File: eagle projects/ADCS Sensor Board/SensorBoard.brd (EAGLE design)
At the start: 91 x 91 mm, 128 parts, among them Q3 CSTCR4M00G15L99, Q5 32.768kHz, U10 LMV321, U2 ADS7841E_2K5, U3 LMV321, U5 ADS7841E_2K5, U6 REF194GSZ-REEL7, U7 TLV9054IDR, U8 LMV321

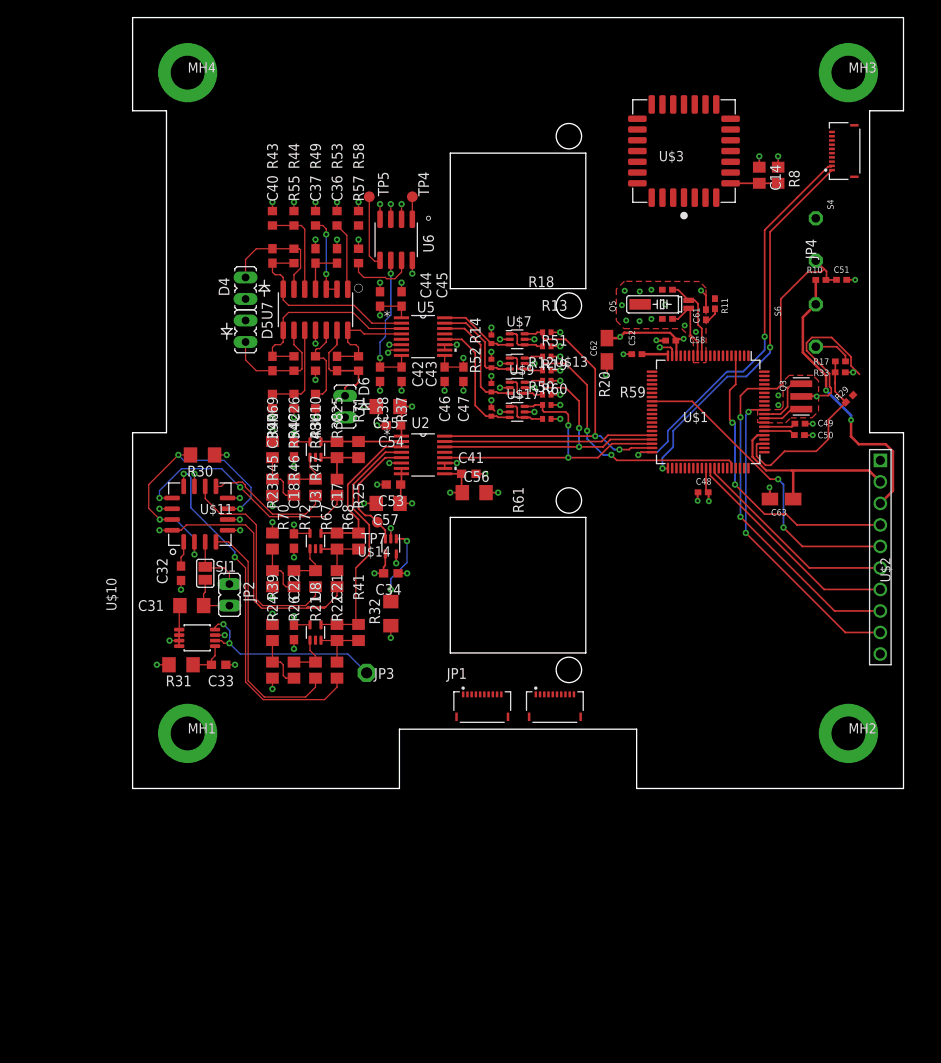
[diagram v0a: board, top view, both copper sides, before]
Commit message: Renamed sensor board files. Added notes to schematic for remaining work
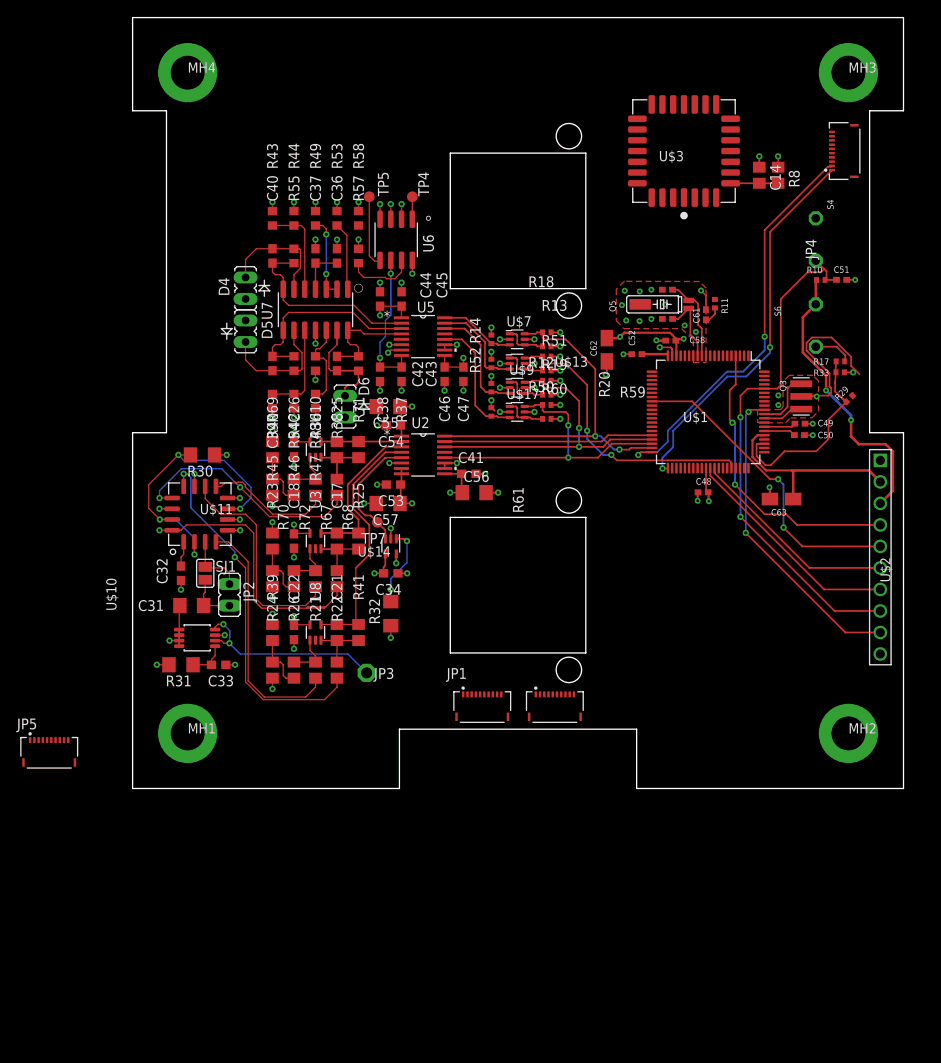
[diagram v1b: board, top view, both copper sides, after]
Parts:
- added JP5: 5034801000, my_library:MOLEX_5034801000
- R10, R11, R17, R29, R33: device rcl:0402 -> rcl:R0402
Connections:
- new net ACT_BRD_3V_PRESENT: JP4.3, JP5.1
- new net ACT_BRD_5V_PRESENT: JP4.4, JP5.2
- new net N$10: JP5.7
- new net N$17: JP5.8
- new net N$18: JP5.9
- new net N$19: JP5.10
- new net N$3: JP5.3
- new net N$4: JP5.4
- new net N$5: JP5.5
- new net N$9: JP5.6
- new net SEN_BRD_3V_PRESENT: JP4.5
- new net SEN_BRD_5V_PRESENT: JP4.6
- net GND: now also JP1.S1, JP1.S2, JP3.S1, JP3.S2, JP4.S1, JP4.S2, JP5.S1, JP5.S2

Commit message: Buncha layout done
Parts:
- removed C40: 9.1p, rcl:C0603
- removed C41, C43, C45, C46, C53, C54: 0.1u, rcl:C0603
- removed C42, C44, C47: 1u, rcl:C0603
- removed C51: 1n, rcl:0402
- removed C55, C56, C57: 1u, resistor:C1206
- removed C62: 10u, rcl:A/3216-18R
- removed D4, D5, D6: SFH2430, my_library:JP1Y_LED_SCREEN
- removed R53, R57, R58: 5.1M, rcl:R0603
- removed R54, R55: 698k, rcl:R0603
- removed R59, R60, R61: 10k, rcl:R0402
- removed R67, R68: 5.6k, rcl:R0805
- removed R69, R70: 1k, rcl:R0805
- removed R71, R72: 1.37M, rcl:R0805
- removed U$10: IRF7507TRPBF, my_library:SOP8P65_300X490X111L53X30N
- removed U$11: HMC1053, my_library:LCCS16P127_736X736X279L127X50N
- removed U$13, U$17, U$7, U$9: BSS138PS,115, my_library:SOT23-6P65_200X110L30X25N_BSS138PS,115
- removed U$14: LM20BIM7X_NOPB, my_library:SOT23-5P65_210X110L40X22N_LM20
- removed U$3: MTI-1, my_library:LCC28P127_1210X1210X260L90X63_MTI-1
- removed U10: LMV321, my_library:SOT23-5P65_210X110L36X22N
- added A1: HMC1053PA0242, my_library:PA0242
- added C10: 1n, rcl:0402
- added C12, C15, C16: 1u, resistor:C1206
- added C13, C19, C23, C30: 0.1u, rcl:C0603
- added C2: 10u, rcl:A/3216-18R
- added C20, C24, C27: 1n, rcl:C0805
- added C28: 470n, rcl:C0805
- added C29: 4.7u, rcl:C0603
- added C35: 1u, rcl:C0603
- added D1, D2, D3: SFH2430, my_library:JP1Y_LED_SCREEN
- added J6: MTI-1_8428-11B1-RK-TP, my_library:PLCC-28_SOCKET_TH
- added Q2: IRF7507TRPBF, my_library:SOP8P65_300X490X111L53X30N
- added Q4, Q6: BSS138PS,115, my_library:SOT23-6P65_200X110L30X25N_BSS138PS,115
- added R1: 0R, rcl:R0402
- added R15: 5.1M, resistor:R1206
- added R16, R9: 5.6k, rcl:R0805
- added R2: 47k, rcl:R0402
- added R27: 27R, rcl:R0805
- added R28, R34: 10k, rcl:R0402
- added R3: 1k4, rcl:R0402
- added R35: 698k, rcl:R0603
- added R4: 100R, rcl:R0402
- added R5: 1M, rcl:R0402
- added R6: 200R, resistor:R1206
- added R7: 1k, rcl:R0805
- added U4: LMV321, my_library:SOT23-5P65_210X110L36X22N
- added U9: ADS7841E_2K5, my_library:DBQ16
- added Y1: 32.768kHz, my_library:MS3V-T1R
- added Y2: CSTCR4M00G15L99, my_library:MURATA-FILTER_CSTCR
- C14: value 470n -> 0.1u; device rcl:C0805 -> rcl:C0603
- C17, C25: value 1n -> 0.1u; device rcl:C0805 -> rcl:C0603
- C21: device rcl:C0805 -> resistor:C1206
- C31: value 1n -> 9.1p; device resistor:C1206 -> rcl:C0603
- C32, C33: value 0.1u -> 9.1p
- C34: value 0.1u -> 1u
- C36: value 4.7u -> 1u
- C38, C39: value 9.1p -> 0.1u
- JP1: value 5034801000 -> (none); device my_library:MOLEX_5034801000 -> jumper:JP1
- JP2: device jumper:JP1 -> pinhead:2X05
- JP3, JP4: value 5034801000 -> (none); device my_library:MOLEX_5034801000 -> pinhead:2X05
- JP5: value 5034801000 -> (none); device my_library:MOLEX_5034801000 -> pinhead:1X04
- Q3: value CSTCR4M00G15L99 -> BSS138PS,115; device murata:MURATA-FILTER_CSTCR -> my_library:SOT23-6P65_200X110L30X25N_BSS138PS,115
- Q5: value 32.768kHz -> BSS138PS,115; device microcrystal:MS3V-T1R -> my_library:SOT23-6P65_200X110L30X25N_BSS138PS,115
- R10: value 47k -> 5.6k; device rcl:R0402 -> rcl:R0805
- R11: value 0R -> 1.37M; device rcl:R0402 -> rcl:R0805
- R12, R18, R19: value 10k -> 1.37M; device rcl:R0402 -> rcl:R0805
- R13, R14, R20: value 10k -> 1k; device rcl:R0402 -> rcl:R0805
- R17: value 100R -> 5.6k; device rcl:R0402 -> rcl:R0805
- R21: value 5.6k -> 1k
- R23: value 1k -> 5.6k
- R24: value 1k -> 1.37M
- R26: value 1.37M -> 5.1M; device rcl:R0805 -> resistor:R1206
- R29: value 1k4 -> 10k
- R30: device resistor:R1206 -> rcl:R0603
- R31: value 200R -> 10k; device resistor:R1206 -> rcl:R0402
- R32: value 5.1M -> 10k; device resistor:R1206 -> rcl:R0402
- R33: value 1M -> 10k
- R36: value 5.6k -> 698k; device rcl:R0805 -> rcl:R0603
- R38: value 5.6k -> 10k; device rcl:R0805 -> rcl:R0402
- R39: value 1k -> 10k; device rcl:R0805 -> rcl:R0402
- R40: value 1k -> 5.1M; device rcl:R0805 -> rcl:R0603
- R41: value 1.37M -> 5.1M; device rcl:R0805 -> rcl:R0603
- R42: value 1.37M -> 10k; device rcl:R0805 -> rcl:R0402
- R43, R45, R46: value 13.7k -> 10k; device rcl:R0603 -> rcl:R0402
- R44: value 13.7k -> 5.1M
- R49: value 5.1M -> 13.7k
- R50, R51, R52: value 10k -> 13.7k; device rcl:R0402 -> rcl:R0603
- R8: value 27R -> 1k
- U2: value ADS7841E_2K5 -> LMV321; device my_library:DBQ16 -> my_library:SOT23-5P65_210X110L36X22N
- U3: value LMV321 -> ADS7841E_2K5; device my_library:SOT23-5P65_210X110L36X22N -> my_library:DBQ16
- U5: value ADS7841E_2K5 -> LM20BIM7X_NOPB; device my_library:DBQ16 -> my_library:SOT23-5P65_210X110L40X22N_LM20
- U6: value REF194GSZ-REEL7 -> LMV321; device my_library:SOIC8P127_490X600X175L83X41N_REF194GSZ-REEL7 -> my_library:SOT23-5P65_210X110L36X22N
- U8: value LMV321 -> REF194GSZ-REEL7; device my_library:SOT23-5P65_210X110L36X22N -> my_library:SOIC8P127_490X600X175L83X41N_REF194GSZ-REEL7
- moved JP5 105.0 mm to (55.9, 87.6)
- moved R8 74.6 mm to (19.4, 24.1)
- moved R17 67.6 mm to (27.0, 13.3), turned to 270 degrees
- moved JP2 65.2 mm to (74.9, 8.26), turned to 90 degrees
- moved R10 65.1 mm to (27.0, 24.1), turned to 270 degrees
- moved R31 60.1 mm to (51.8, 53.2), turned to 0 degrees
- moved R11 57.4 mm to (21.9, 24.1)
- moved R41 55.1 mm to (30.8, 73.3), turned to 180 degrees
- moved U8 54.7 mm to (24.8, 73.0), turned to 270 degrees
- moved JP4 51.8 mm to (62.9, 27.3), turned to 180 degrees
- moved R40 49.9 mm to (29.2, 62.2), turned to 90 degrees
- moved C33 48.5 mm to (19.4, 62.2), turned to 270 degrees
- moved C14 47.7 mm to (42.5, 36.5), turned to 0 degrees
- moved R42 46.8 mm to (51.8, 47.5), turned to 0 degrees
- moved R13 46.6 mm to (19.4, 17.8), turned to 270 degrees
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- renumbered C48 to C7, C49 to C11, C50 to C8, C52 to C6, C58 to C3, C59 to C5, C60 to C4, C61 to C1, C63 to C9, S4 to S1, S6 to S2, U$1 to U1, U$2 to J5
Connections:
- removed net N$10: JP5.7
- removed net N$11: JP3.7
- removed net N$13: JP3.8
- removed net N$15: JP3.9
- removed net N$16: JP3.10
- removed net N$17: JP5.8
- removed net N$18: JP5.9
- removed net N$19: JP5.10
- removed net N$3: JP5.3
- removed net N$4: JP5.4
- removed net N$5: JP5.5
- removed net N$6: JP1.6
- removed net N$8: JP1.7
- removed net N$9: JP5.6
- removed net P6.4: U1.1
- new net INIT_EPS_BURN_WIRE: JP5.3, U1.54
- net !CS!_HMC1053: now also U3.15; no longer U$3.9, U2.15
- net !CS!_MTI: now also J6.9
- net !CS!_SUN_X+: now also JP2.10; no longer JP1.1
- net !CS!_SUN_X-: now also JP2.8; no longer JP1.2
- net !CS!_SUN_Y+: now also JP2.4; no longer JP1.4
- net !CS!_SUN_Y-: now also JP2.2; no longer JP1.5
- net !CS!_SUN_Z-: now also JP2.6, Q6.6, R43.1; no longer JP1.3, R51.1, U$13.6
- net +3V3: now also A1.1, C12.1, C14.1, C15.1, C16.1, C17.1, C19.1, C2.+, C23.1, C25.2, J6.15, J6.7, JP5.2, Q3.2, Q3.5, Q4.2, Q4.5, Q5.2, Q5.5, Q6.2, Q6.5, R1.2, R13.1, R2.2, R20.1, R27.1, R28.1, R29.1, R32.2, R38.1, R42.2, R43.2, R6.2, R7.1, U2.5, U3.1, U3.7, U3.8, U3.9, U4.5, U5.4, U6.5; no longer C32.1, C34.2, C41.1, C53.1, C54.1, C55.1, C56.1, C57.1, C62.+, R10.2, R11.2, R12.1, R13.2, R18.1, R19.2, R23.1, R50.1, R51.2, R59.1, R60.2, R69.1, R8.1, U$11.1, U$13.2, U$13.5, U$14.4, U$17.2, U$17.5, U$3.15, U$3.7, U$7.2, U$7.5, U$9.2, U$9.5, U10.5, U2.1, U2.7, U2.8, U2.9, U3.5, U8.5
- net +4V5: now also C34.1, C39.1, U8.6, U9.8; no longer C42.1, C43.1, U5.8, U6.6
- net +5V: now also C29.1, C30.1, C35.1, C38.1, JP5.1, R33.2, R34.2, R45.2, R47.2, R49.2, R51.2, U8.2, U8.3, U9.1, U9.7, U9.9; no longer C44.1, C45.1, C46.1, C47.1, R14.2, R20.2, R44.2, R48.2, R52.2, R61.2, U5.1, U5.7, U5.9, U6.2, U6.3
- net 0_DEGREES: now also C33.2, R37.2, U9.2; no longer C40.2, R55.2, U5.2
- net 120_DEGREES: now also C32.2, R36.2, U9.3; no longer C39.2, R54.2, U5.3
- net 240_DEGREES: now also C31.2, R35.2, U9.4; no longer C38.2, R37.2, U5.4
- net 5V_!CS!_SUN_Z-: now also Q6.3, R46.1, U9.15; no longer R52.1, U$13.3, U5.15
- net 5V_SPI_CLK: now also Q3.3, R33.1, U9.16; no longer R14.1, U$7.3, U5.16
- net 5V_SPI_MISO: now also Q4.3, R34.1, U9.12; no longer R61.1, U$17.3, U5.12
- net 5V_SPI_MOSI: now also Q5.3, R45.1, U9.14; no longer R20.1, U$9.3, U5.14
- net ACT_BRD_3V_PRESENT: now also JP4.7; no longer JP4.3, JP5.1
- net ACT_BRD_5V_PRESENT: now also JP4.5; no longer JP4.4, JP5.2
- net AVCC1: now also R1.1; no longer R11.1
- net BRD_TEMP_MEAS: now also U3.5, U5.3; no longer U$14.3, U2.5
- net B_MEAS_X: now also C24.2, R19.1, U3.4, U4.4; no longer C21.2, R41.1, U2.4, U8.4
- net B_MEAS_Y: now also C20.2, R12.1, U2.4, U3.3; no longer C17.2, R25.1, U2.3, U3.4
- net B_MEAS_Z: now also C27.2, R25.1, U3.2, U6.4; no longer C25.2, R71.1, U10.4, U2.2
- net GND: now also A1.11, A1.14, A1.5, A1.8, C10.2, C12.2, C13.1, C14.2, C15.2, C16.2, C17.2, C19.2, C2.-, C23.2, C25.1, C28.1, C29.2, C30.2, C34.2, C35.2, C38.2, C39.2, D1.2, D2.2, D3.2, J6.13, J6.25, J6.4, J6.8, JP5.4, Q2.3, R14.2, R15.1, R21.2, R26.1, R41.1, R44.1, R48.1, R5.1, R50.1, R52.1, R8.2, U2.2, U3.10, U3.11, U3.6, U4.2, U5.2, U5.5, U6.2, U8.4, U9.10, U9.11, U9.6, Y1.P3, Y2.2; no longer C14.1, C32.2, C33.1, C34.1, C41.2, C42.2, C43.2, C44.2, C45.2, C46.2, C47.2, C51.2, C53.2, C54.2, C55.2, C56.2, C57.2, C62.-, D4.2, D5.2, D6.2, JP1.S1, JP1.S2, JP3.S1, JP3.S2, JP4.S1, JP4.S2, JP5.S1, JP5.S2, Q3.2, Q5.P3, R24.2, R32.1, R33.1, R43.1, R45.1, R47.1, R49.1, R53.2, R57.1, R58.1, R70.2, U$10.3, U$11.11, U$11.14, U$11.5, U$11.8, U$14.2, U$14.5, U$3.13, U$3.25, U$3.4, U$3.8, U10.2, U2.10, U2.11, U2.6, U3.2, U5.10, U5.11, U5.6, U6.4, U8.2
- net HMC1053_RESET: now also Q2.2, Q2.4, U1.1; no longer U$10.2, U$10.4
- net IN2+BIAS: now also R47.1, R48.2; no longer R43.2, R44.1
- net IN3+BIAS: now also R49.1, R50.2; no longer R45.2, R46.1
- net IN4+BIAS: now also R51.1, R52.2; no longer R47.2, R48.1
- net MAG_Y_FIN: now also JP3.6; no longer JP3.3
- net MAG_Y_RIN: now also JP3.8; no longer JP3.4
- net MAG_Z_FIN: now also JP3.10, JP3.2; no longer JP3.1, JP3.5
- net MAG_Z_RIN: now also JP3.4, JP3.9; no longer JP3.2, JP3.6
- net MTI_DRDY: now also J6.22; no longer U$3.22
- net N$12: now also R4.1; no longer R17.1
- net N$14: now also Q3.1, Q3.4, R28.2; no longer R12.2, U$7.1, U$7.4
- net N$20: now also R11.1, R7.2, R8.1; no longer R23.2, R24.1, R26.1
- net N$21: now also C20.1, R10.1, R12.2, U2.3; no longer C17.1, R22.1, R25.2, U3.3
- net N$23: now also R11.2, R9.1, U2.1; no longer R21.1, R26.2, U3.1
- net N$26: now also R30.2; no longer R49.2
- net N$27: now also R40.1; no longer R53.1
- net N$28: now also C31.1, D3.1, R35.1; no longer C38.1, D6.1, R37.1
- net N$30: now also Q5.1, Q5.4, R38.2; no longer R18.2, U$9.1, U$9.4
- net N$31: now also C32.1, D2.1, R36.1; no longer C39.1, D5.1, R54.1
- net N$32: now also C33.1, D1.1, R37.1; no longer C40.1, D4.1, R55.1
- net N$33: now also U8.5; no longer U6.5
- net N$34: now also U8.1; no longer U6.1
- net N$35: now also C21.2, JP1.2; no longer C31.2, JP2.2
- net N$36: now also A1.15, A1.2, A1.7, R15.2; no longer R30.2, U$11.15, U$11.2, U$11.7
- net N$37: now also A1.3, A1.6, JP1.1; no longer JP2.1, U$11.3, U$11.6
- net N$38: now also C21.1, Q2.5, Q2.6, Q2.7, Q2.8; no longer C31.1, U$10.5, U$10.6, U$10.7, U$10.8
- net N$39: now also C13.2, Q2.1, R6.1; no longer C33.2, R31.1, U$10.1
- net N$40: now also R26.2, U5.1; no longer R32.2, U$14.1
- net N$41: now also R41.2, U8.7; no longer R57.2, U6.7
- net N$42: now also Q6.1, Q6.4, R39.2; no longer R50.2, U$13.1, U$13.4
- net N$43: now also R44.2, U8.8; no longer R58.2, U6.8
- net N$48: now also Q4.1, Q4.4, R29.2; no longer R59.2, U$17.1, U$17.4
- net N$49: now also R13.2, R14.1, R18.1; no longer R39.2, R40.1, R42.1
- net N$50: now also C24.1, R17.1, R19.2, U4.3; no longer C21.1, R38.1, R41.2, U8.3
- net N$52: now also R16.1, R18.2, U4.1; no longer R36.1, R42.2, U8.1
- net N$59: now also R20.2, R21.1, R24.1; no longer R69.2, R70.1, R72.1
- net N$60: now also C27.1, R23.1, R25.2, U6.3; no longer C25.1, R68.1, R71.2, U10.3
- net N$62: now also R22.1, R24.2, U6.1; no longer R67.1, R72.2, U10.1
- net N$7: now also C28.2, J6.5, R27.2; no longer C14.2, R8.2, U$3.5
- net OUT_A_N: now also A1.10, R9.2; no longer R21.2, U$11.10
- net OUT_A_P: now also A1.16, R10.2; no longer R22.2, U$11.16
- net OUT_B_N: now also A1.4, R16.2; no longer R36.2, U$11.4
- net OUT_B_P: now also A1.12, R17.2; no longer R38.2, U$11.12
- net OUT_C_N: now also A1.9, R22.2; no longer R67.2, U$11.9
- net OUT_C_P: now also A1.13, R23.2; no longer R68.2, U$11.13
- net P5.2/XT2IN1: now also Y2.3; no longer Q3.3
- net P5.3/XT2OUT1: now also Y2.1; no longer Q3.1
- net P5.4/XIN1: now also Y1.P2; no longer Q5.P2
- net P5.5/XOUT1: now also Y1.P1; no longer Q5.P1
- net RST/SBWTDIO: now also C10.1, R2.1; no longer C51.1, R10.1
- net SEN_BRD_3V_PRESENT: now also JP4.3; no longer JP4.5
- net SEN_BRD_5V_PRESENT: now also JP4.1; no longer JP4.6
- net TARGET_DP: now also R3.2; no longer R29.2
- net TARGET_PUR: now also R3.1, R4.2, R5.2; no longer R17.2, R29.1, R33.2
- net UCA0RXD: now also JP4.10; no longer JP4.1
- net UCA0TXD: now also JP4.8; no longer JP4.2
- net UCB0_SPI_CLK: now also J6.12, JP2.1, Q3.6, R31.1, U3.16; no longer JP1.10, R13.1, U$3.12, U$7.6, U2.16
- net UCB0_SPI_MISO: now also J6.11, JP2.3, Q4.6, R32.1, U3.12; no longer JP1.9, R60.1, U$17.6, U$3.11, U2.12
- net UCB0_SPI_MOSI: now also J6.10, JP2.5, Q5.6, R42.1, U3.14; no longer JP1.8, R19.1, U$3.10, U$9.6, U2.14
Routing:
- net !CS!_MTI: track 0.00 -> 48.1 mm
- net MTI_DRDY: track 0.00 -> 43.6 mm, vias 0 -> 3
- net UCB0_SPI_MISO: track 36.5 -> 79.3 mm, vias 2 -> 4
- net UCB0_SPI_CLK: track 43.7 -> 84.5 mm
- net UCB0_SPI_MOSI: track 38.1 -> 77.0 mm, vias 2 -> 4
- net HMC1053_RESET: track 23.5 -> 52.5 mm
- net GND: track 94.6 -> 70.3 mm, vias 70 -> 67
- net UCA0TXD: track 47.8 -> 23.8 mm
- net UCA0RXD: track 45.5 -> 22.6 mm
- net N$37: track 9.48 -> 24.6 mm, vias 1 -> 0
- net MAG_Z_FIN: track 0.00 -> 13.7 mm, vias 0 -> 1
- net +4V5: track 17.0 -> 30.2 mm
- net OUT_C_P: track 28.4 -> 15.7 mm, vias 2 -> 1
- net OUT_A_N: track 26.4 -> 14.1 mm, vias 0 -> 1
- net MAG_Z_RIN: track 0.00 -> 12.0 mm, vias 0 -> 1
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- added copper zone on layer 15, net +3V3
- added copper zone on layer 15, net +5V
- added copper zone on layer 15, net +GND
- added copper zone on layer 15, net GND
- added copper zone on layer 2, net GND
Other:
- outline, holes or cut-outs redrawn
- board text added: "CTS<<"
- board text added: "Designed by T. Christison"
- board text added: "LORIS ADCS SENSOR BOARD - REV A"
- board text added: "Q3"
- board text added: "Q4"
- board text added: "Q5"
- board text added: "Q6"
- board text added: "RTS>>"
- board text added: "RXD<<"
- board text added: "SBWRST"
- board text added: "SBWTST"
- board text added: "TXD>>"
- board text added: "U2"
- board text added: "U4"
- board text added: "U6"
- board text removed: "CTS <<"
- board text removed: "RTS >>"
- board text removed: "RXD <<"
- board text removed: "SBW RST"
- board text removed: "SBW TST"
- board text removed: "TXD >>"

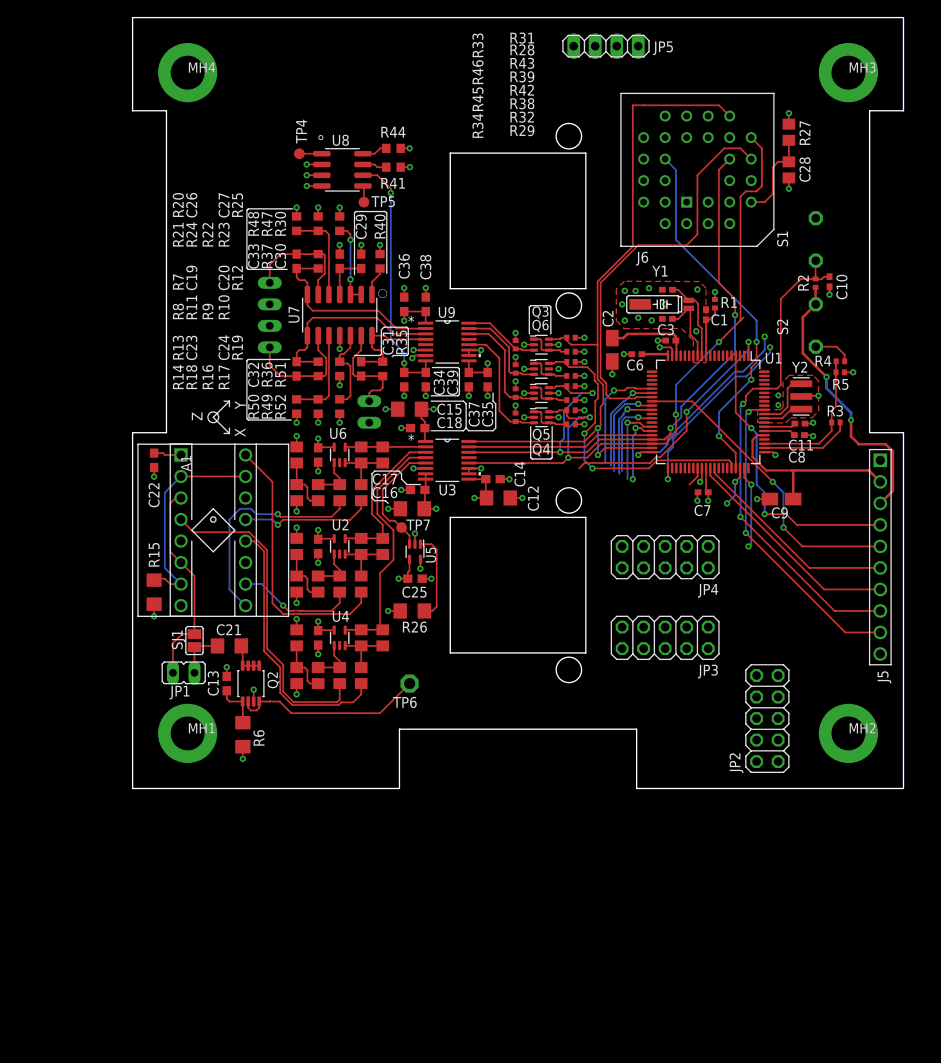
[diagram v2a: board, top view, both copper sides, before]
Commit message: Board update commit before removing Z+ sunsensor from layout
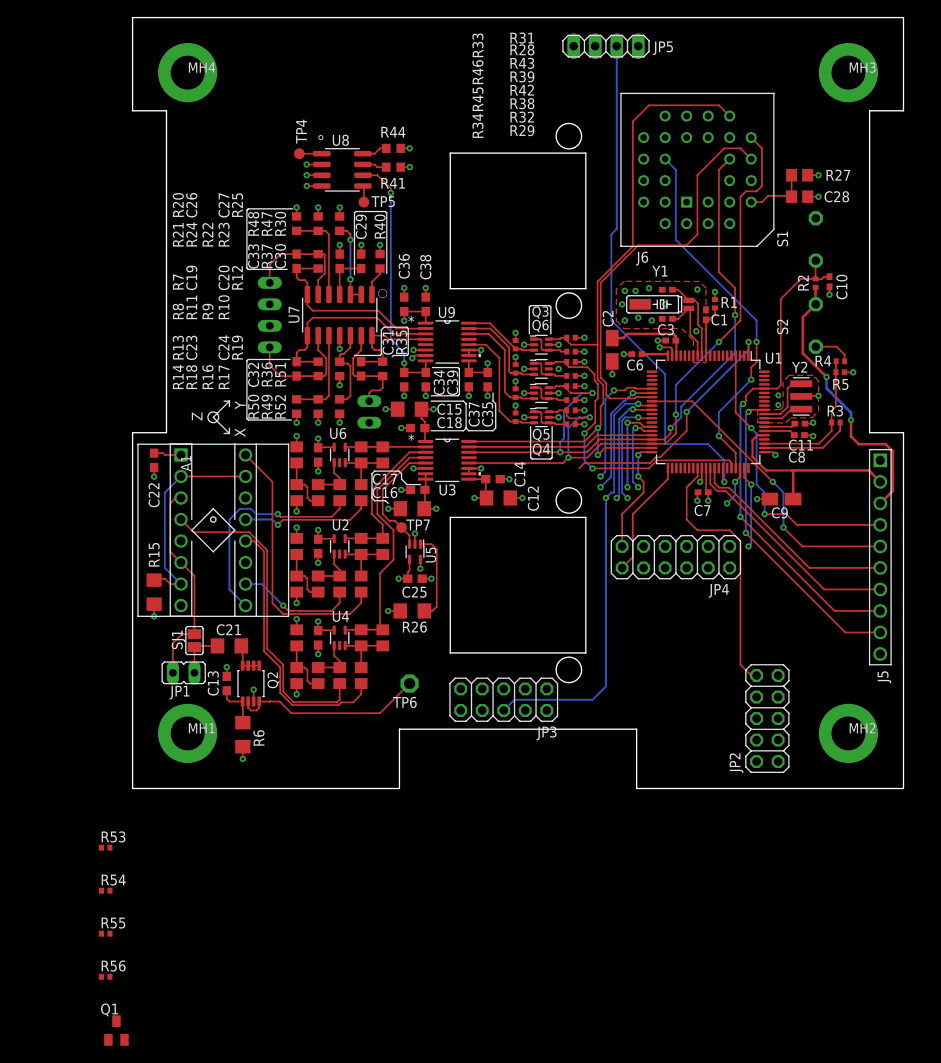
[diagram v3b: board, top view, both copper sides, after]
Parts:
- added Q1: BC850SMD, transistor-npn:SOT23-BEC
- added R53, R55: 1k, rcl:R0402
- added R54, R56: 2k, rcl:R0402
- JP4: device pinhead:2X05 -> pinhead:2X06
- moved JP3 20.4 mm to (43.8, 10.5)
- moved R27 5.24 mm to (78.7, 72.4), turned to 180 degrees
- moved C28 3.42 mm to (78.7, 69.8), turned to 180 degrees
- moved JP4 1.27 mm to (64.1, 27.3)
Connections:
- removed net SEN_BRD_3V_PRESENT: JP4.3
- new net ACT_BRD_5V_SHIFTED: JP4.5, R55.1, R56.2
- new net MSP430_ACTIVE: JP4.10
- new net MSP_OBC_RESET: JP4.9
- new net N$1: Q1.B
- new net RESERVED_1: JP4.2
- new net RESERVED_2: JP4.4
- new net RESERVED_3: JP4.6
- new net RESERVED_4: JP4.8
- net +3V3: now also JP4.3
- net +5V: now also R53.2
- net ACT_BRD_3V_PRESENT: now also JP3.7
- net ACT_BRD_5V_PRESENT: now also JP3.5, R55.2; no longer JP4.5
- net GND: now also Q1.E, R54.1, R56.1
- net RST/SBWTDIO: now also Q1.C
- net SEN_BRD_5V_PRESENT: now also R53.1, R54.2
- net UCA0RXD: now also JP4.12; no longer JP4.10
- net UCA0TXD: now also JP4.11; no longer JP4.8
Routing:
- net INIT_EPS_BURN_WIRE: track 0.00 -> 61.9 mm, vias 0 -> 1
- net MAG_Y_FIN: track 11.7 -> 51.0 mm, vias 1 -> 2
- net !CS!_SUN_X+: track 2.37 -> 31.0 mm
- net UCA0TXD: track 23.8 -> 13.9 mm
- net UCA0RXD: track 22.6 -> 14.4 mm, vias 2 -> 0
- net !CS!_SUN_Z+: track 9.71 -> 13.1 mm, vias 1 -> 2
- net N$7: track 10.8 -> 7.69 mm
- net MAG_Z_RIN: track 12.0 -> 15.0 mm, vias 1 -> 2
- net MAG_Y_RIN: track 11.0 -> 13.8 mm, vias 1 -> 2
- net MAG_Z_FIN: track 13.7 -> 15.5 mm, vias 1 -> 2
- net !CS!_SUN_Y+: track 8.25 -> 9.46 mm
- net UCB0_SPI_CLK: track 84.5 -> 83.4 mm
- net MAG_X_RIN: track 9.76 -> 10.7 mm, vias 1 -> 2
- net P4.5/UCA1RXD: track 24.8 -> 25.5 mm
- net P4.4/UCA1TXD: track 26.5 -> 27.1 mm
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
